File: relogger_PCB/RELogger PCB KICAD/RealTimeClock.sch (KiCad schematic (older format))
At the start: 12 parts, among them P25 OSC_TRIM, U2 PCF8563, X2 32.768kHz

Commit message: Schematic uploaded with Arduino Nano, SD Card connector and DS3231 connector
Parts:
- removed C6: 1F, symbol CP1
- removed C7: 100n, symbol C
- removed C8: CTRIM, symbol CTRIM-RESCUE-RELogger_PCB_v1
- removed D9: 1N4148, symbol DIODE
- removed P25: OSC_TRIM, symbol CONN_01X01
- removed R10: 10, symbol R
- removed R11, R12, R13, R14: 10k, symbol R-RESCUE-RELogger_PCB_v1
- removed U2: PCF8563, symbol PCF8563-RESCUE-RELogger_PCB_v1
- removed X2: 32.768kHz, symbol QUARTZCMS4_watchXTAL
- added J1: CONN_01X06, symbol CONN_01X06
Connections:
- net labels added: D2/SQW
- net labels removed: D2/INT
- wire segments 39 -> 5
- no-connect marks 0 -> 1
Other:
- note removed: "This needs set-up with accurate clock.\nMaybe use DS3231?"

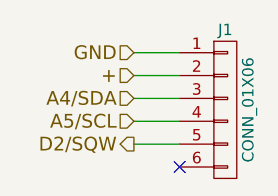
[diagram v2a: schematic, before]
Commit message: Schematic update and PCB initial run
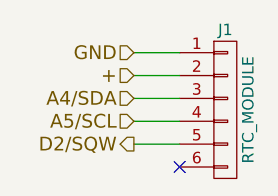
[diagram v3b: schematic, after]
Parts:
- J1: value CONN_01X06 -> RTC_MODULE; footprint (none) -> REInnovationFootprint:TH_RTC_MODULE
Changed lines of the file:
@@
 P 5950 3300
 F 0 "J1" H 5950 3650 50  0000 C CNN
-F 1 "CONN_01X06" V 6050 3300 50  0000 C CNN
-F 2 "" H 5950 3300 50  0001 C CNN
+F 1 "RTC_MODULE" V 6050 3300 50  0000 C CNN
+F 2 "REInnovationFootprint:TH_RTC_MODULE" H 5950 3300 50  0001 C CNN
 F 3 "" H 5950 3300 50  0001 C CNN
 	1    5950 3300
